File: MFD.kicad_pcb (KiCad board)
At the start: 2 copper layers, 209.6 x 209.6 mm, 43 parts, among them U1 4051, U2 ProMicro

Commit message: Adds OpenHardware Logo and GitHub link
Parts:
- added REF**: OSHW-Logo_7.5x8mm_SilkScreen, Symbol:OSHW-Logo_7.5x8mm_SilkScreen, F.Cu at (163.0, 52.2)
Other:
- board text added: "JLCJLCJLCJLC"
- board text added: "https://github.com/FalcoGer/AH64MFD-PCB"

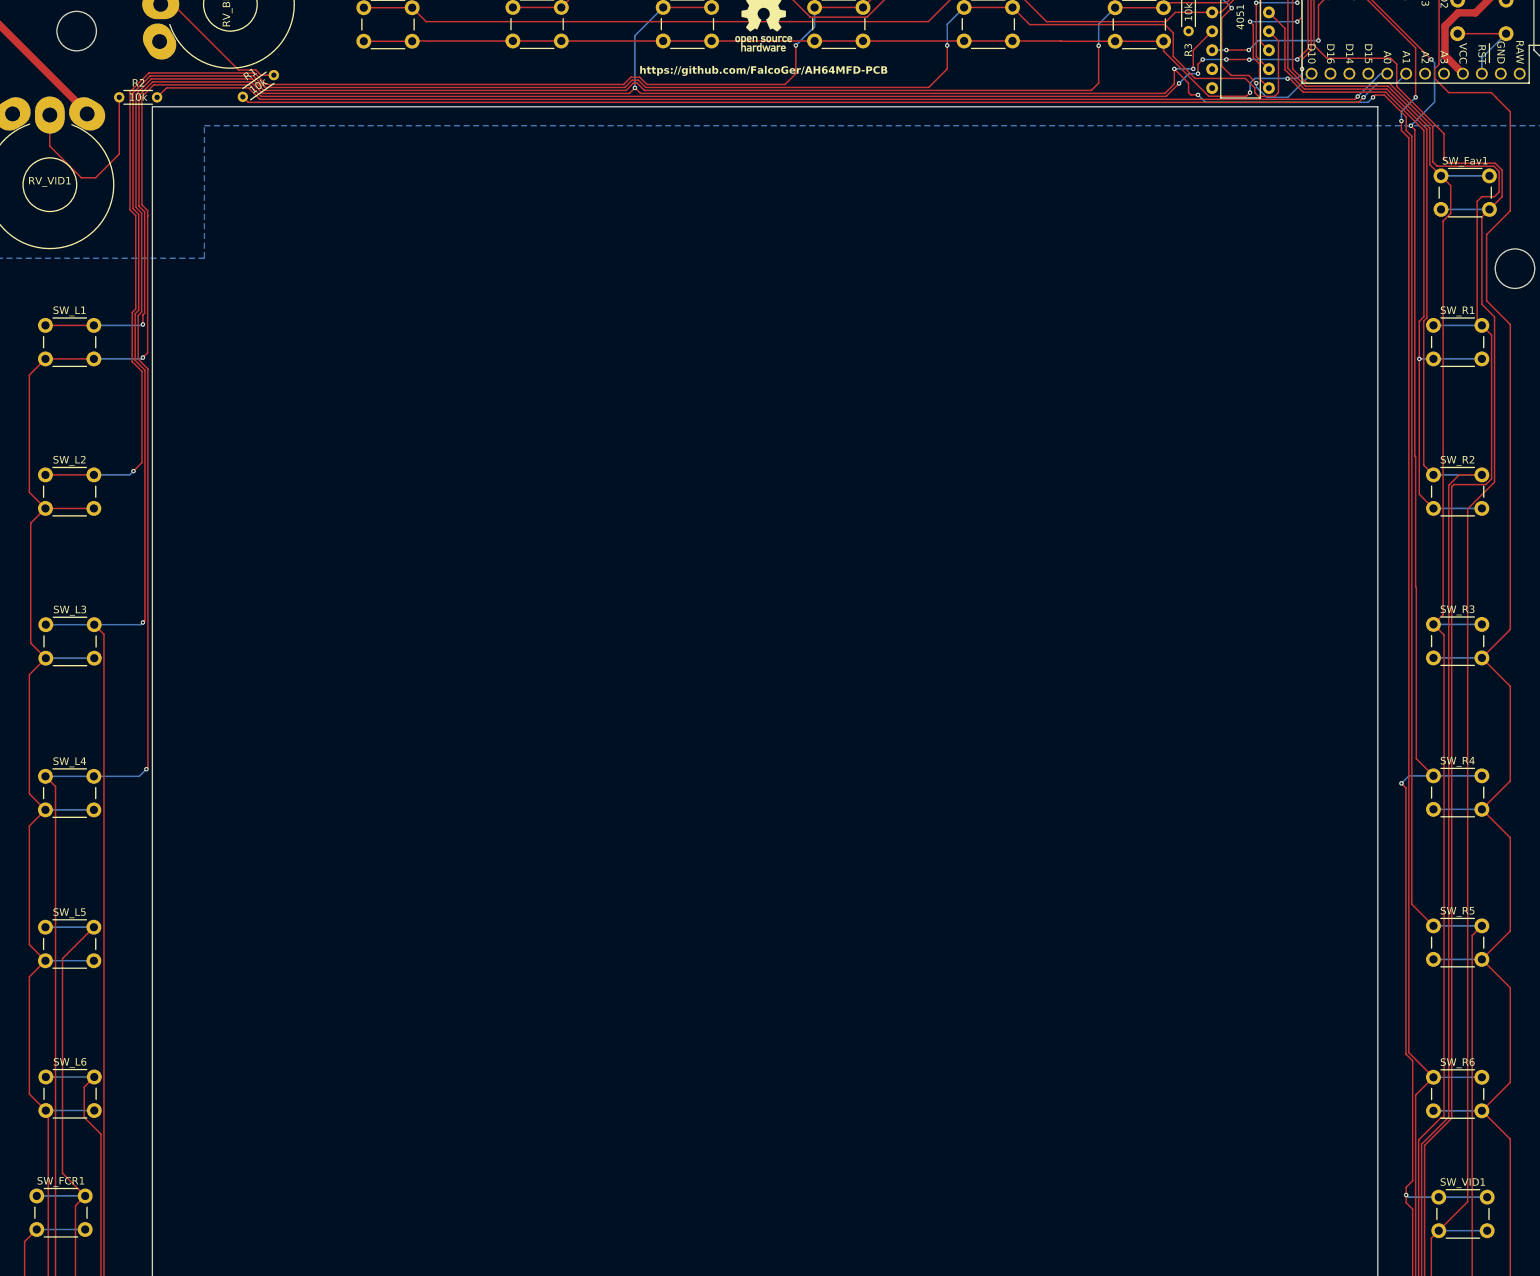
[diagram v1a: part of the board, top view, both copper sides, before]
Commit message: rerouted some tracks to use less vias.
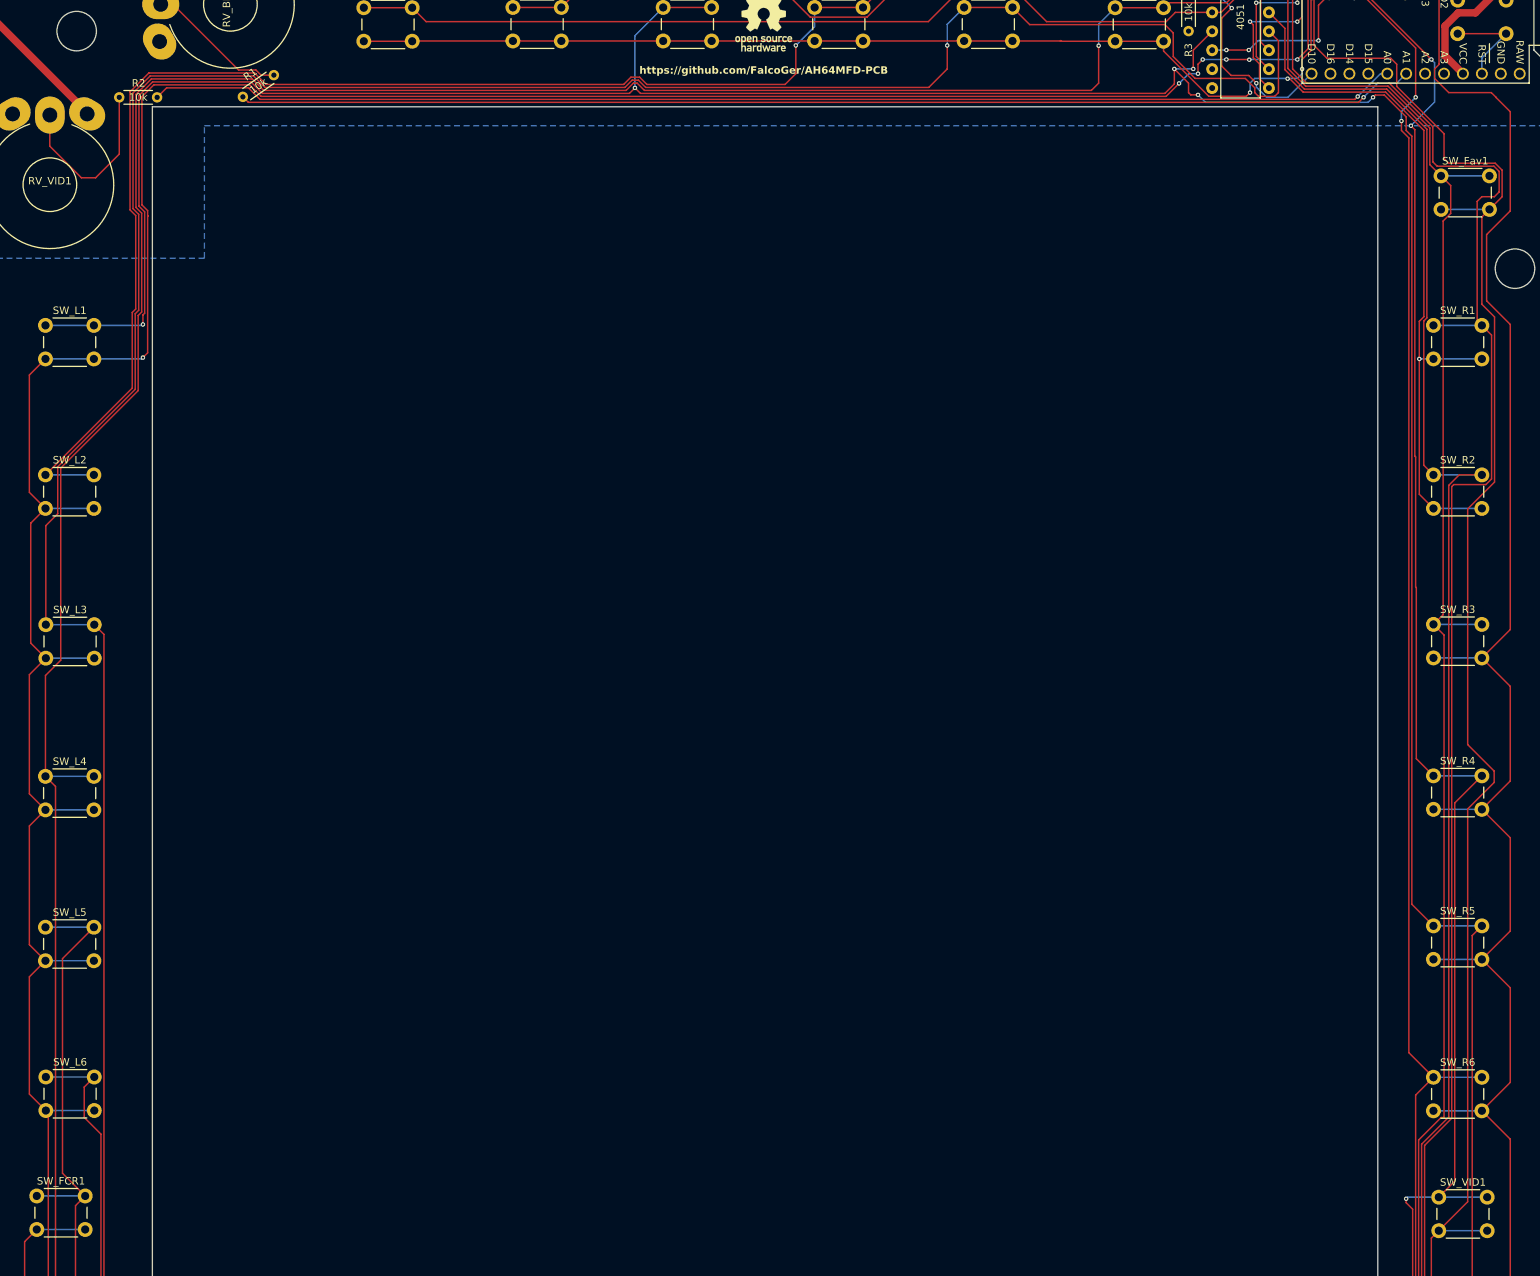
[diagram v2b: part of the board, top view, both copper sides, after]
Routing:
- net Net-(U2-D5): track 483.5 -> 486.4 mm
- net Net-(U1-X6): track 378.4 -> 375.9 mm, vias 8 -> 7
- net Net-(U1-X3): track 406.9 -> 404.9 mm, vias 2 -> 1
- net Net-(U1-X2): track 423.0 -> 421.0 mm, vias 2 -> 1
- net Net-(U1-X4): track 464.4 -> 463.2 mm, vias 8 -> 7

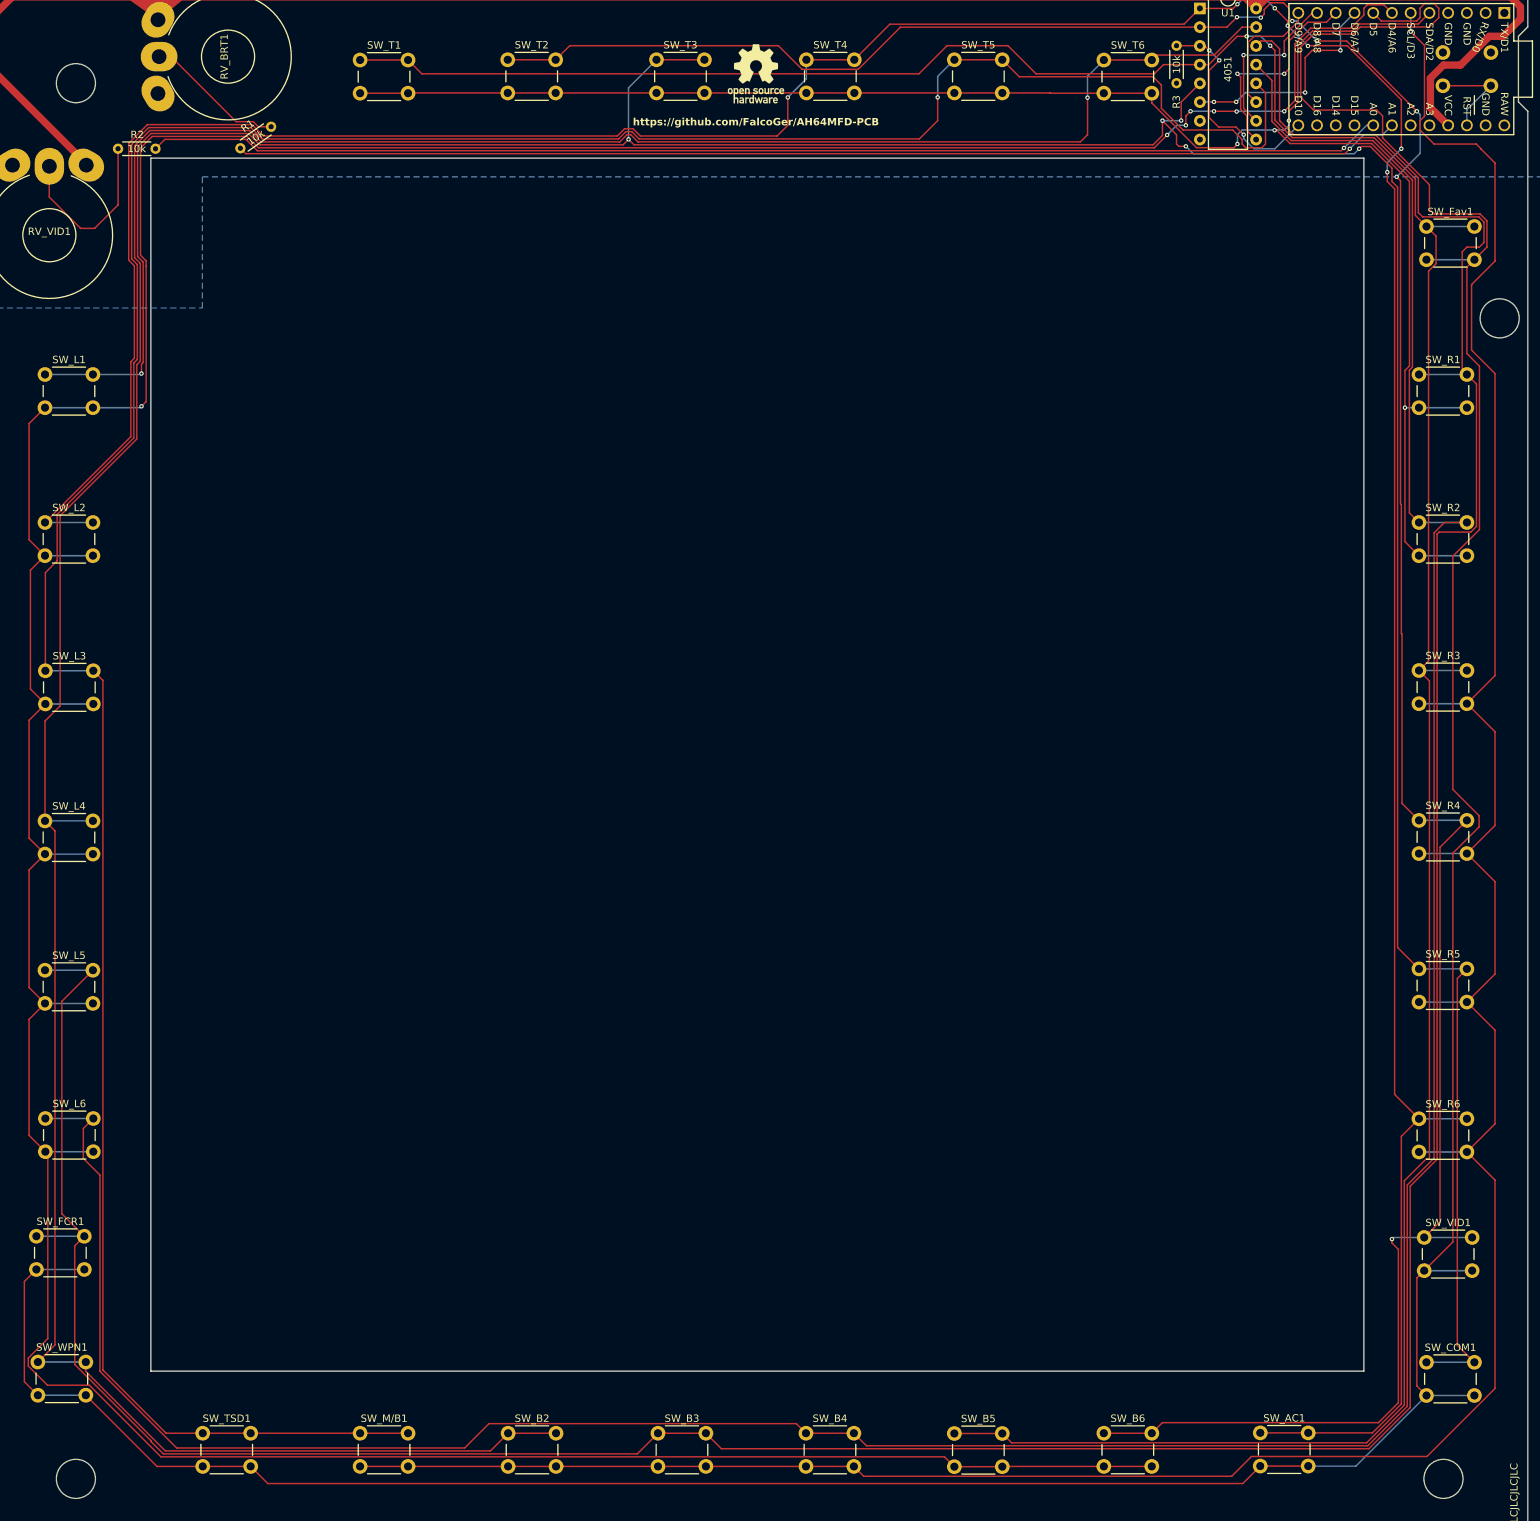
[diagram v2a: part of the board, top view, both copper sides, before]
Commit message: Adds mounting holes to schematic\nReroutes some tracks
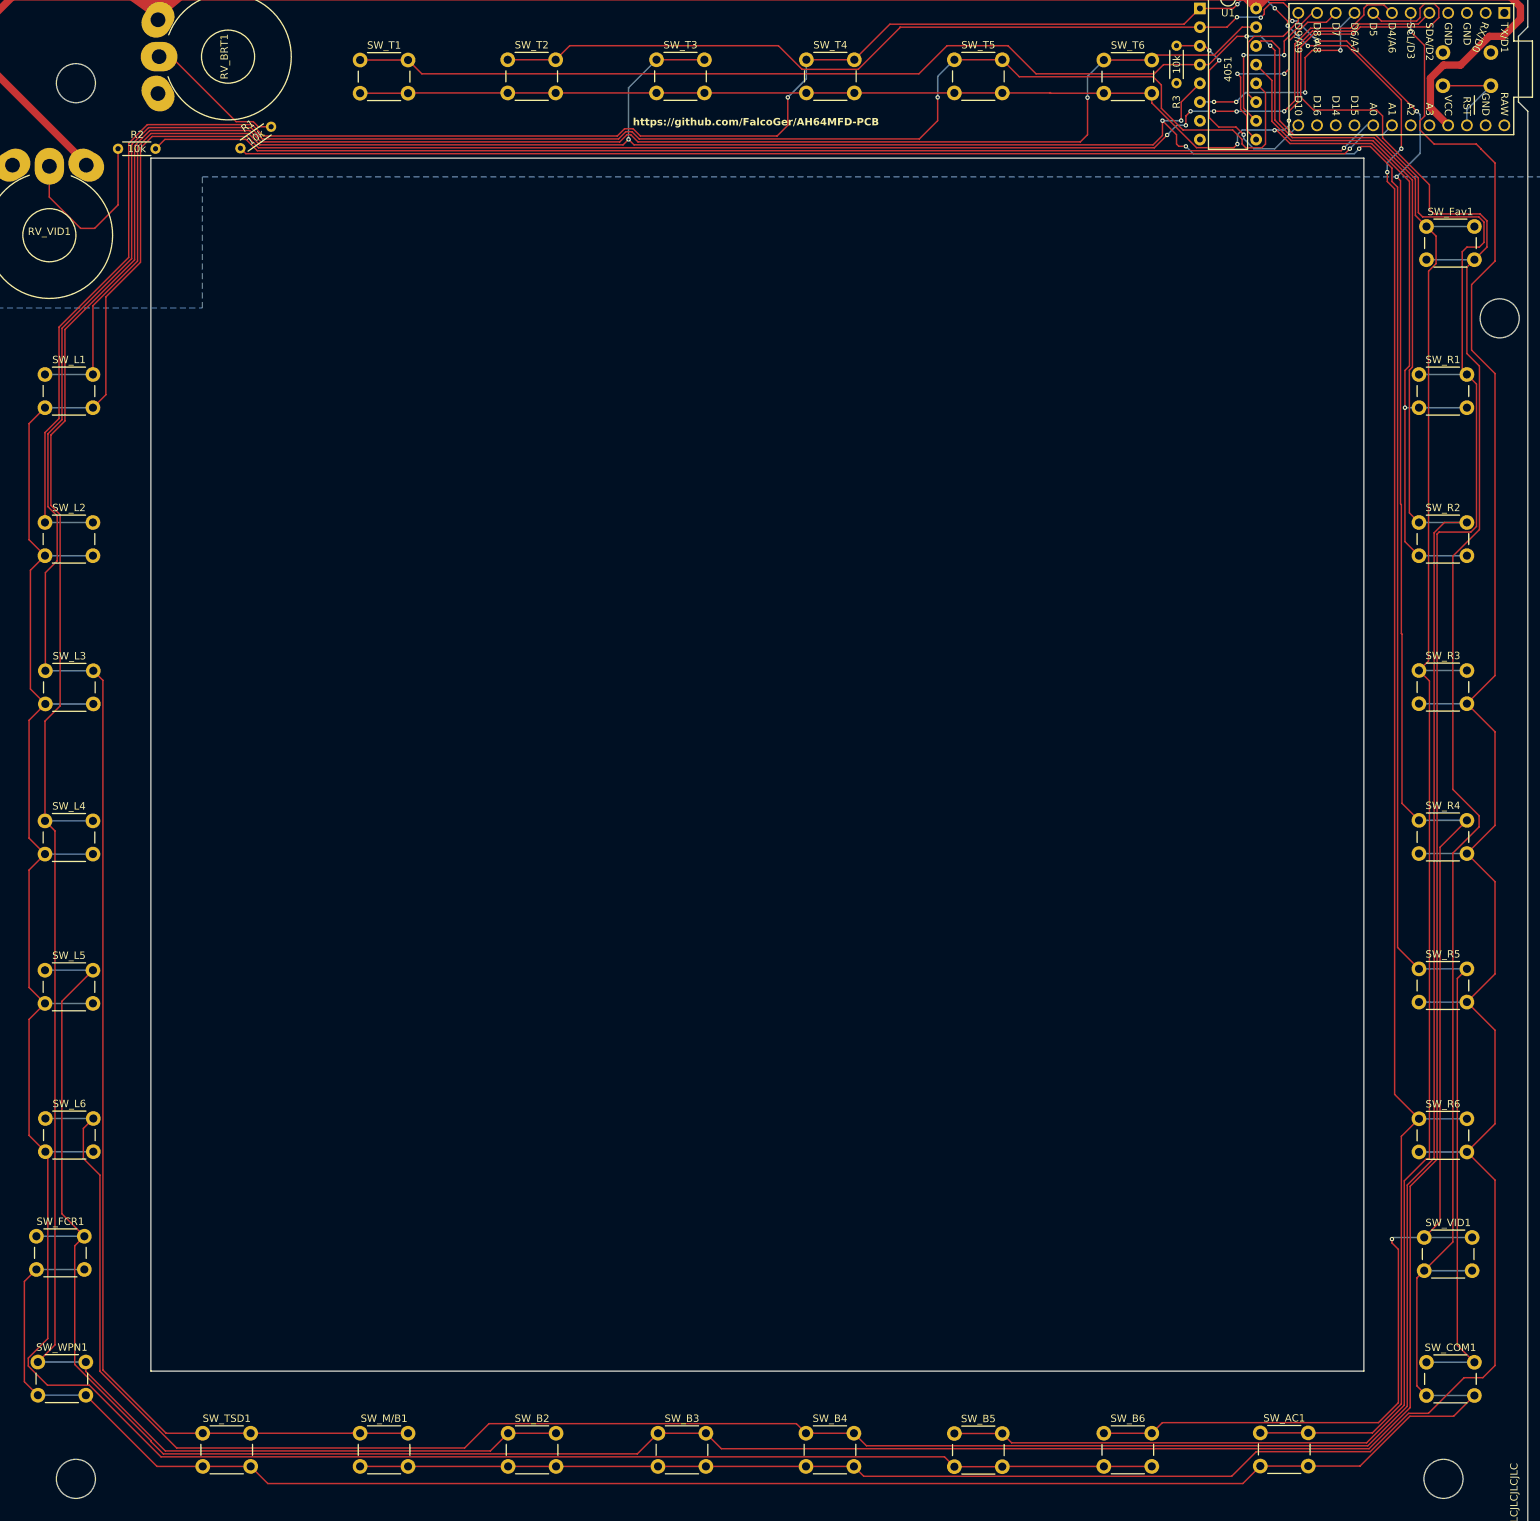
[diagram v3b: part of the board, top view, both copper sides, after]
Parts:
- removed REF**: OSHW-Logo_7.5x8mm_SilkScreen, Symbol:OSHW-Logo_7.5x8mm_SilkScreen
- H1, H2, H3, H4: renamed from REF**; value MountingHole_5.3mm_M5 -> MountingHole
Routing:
- net Net-(U2-D5): track 486.4 -> 492.9 mm
- net Net-(U1-X5): track 428.5 -> 424.1 mm, vias 6 -> 5
- net Net-(U2-D4/A6): track 564.0 -> 559.6 mm, vias 7 -> 6
- net Net-(U2-SCL/D3): track 395.7 -> 393.9 mm
- net Net-(U1-X4): track 463.2 -> 462.6 mm

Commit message: Ground plane over everything Rerouted some tracks, less vias
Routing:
- net Net-(U1-X3): track 405.3 -> 408.6 mm, vias 1 -> 0
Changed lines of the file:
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@@
 	)
 	(segment
-		(start 196.427999 54.800002)
-		(end 189.927999 54.800002)
-		(width 0.2)
-		(layer "F.Cu")
-		(net 6)
-	)
-	(segment
 		(start 216.695999 56.151637)
 		(end 222.764364 62.220002)
@@
 	)
 	(segment
+		(start 196.427999 54.800002)
+		(end 189.927999 54.800002)
+		(width 0.2)
+		(layer "B.Cu")
+		(net 6)
+	)
+	(segment
 		(start 259.419999 117.538002)
 		(end 252.919999 117.538002)
@@
 	)
 	(segment
+		(start 191.728999 52.101002)
+		(end 191.728999 57.031002)
+		(width 0.2)
+		(layer "F.Cu")
+		(net 29)
+	)
+	(segment
+		(start 187.724999 61.035002)
+		(end 184.870999 61.035002)
+		(width 0.2)
+		(layer "F.Cu")
+		(net 29)
+	)
+	(segment
 		(start 68.938999 99.106688)
 		(end 67.033999 101.011688)
@@
 	)
 	(segment
-		(start 187.664999 58.555002)
-		(end 185.184999 61.035002)
-		(width 0.2)
-		(layer "F.Cu")
-		(net 29)
-	)
-	(segment
 		(start 68.284999 118.245002)
 		(end 66.685999 119.844002)
@@
 	)
 	(segment
+		(start 191.728999 57.031002)
+		(end 187.724999 61.035002)
+		(width 0.2)
+		(layer "F.Cu")
+		(net 29)
+	)
+	(segment
 		(start 144.400784 61.035002)
 		(end 96.087057 61.035002)
@@
 	)
 	(segment
+		(start 189.927999 50.300002)
+		(end 191.728999 52.101002)
+		(width 0.2)
+		(layer "F.Cu")
+		(net 29)
+	)
+	(segment
 		(start 88.021999 236.518002)
 		(end 94.521999 236.518002)
@@
 	)
 	(segment
-		(start 189.927999 50.300002)
-		(end 196.427999 50.300002)
-		(width 0.2)
-		(layer "F.Cu")
-		(net 29)
-	)
-	(segment
-		(start 187.664999 55.400002)
-		(end 187.664999 58.555002)
-		(width 0.2)
-		(layer "F.Cu")
-		(net 29)
-	)
-	(segment
 		(start 83.052999 236.518002)
 		(end 88.021999 236.518002)
@@
 		(net 29)
 	)
-	(via
-		(at 187.664999 55.400002)
-		(size 0.6)
-		(drill 0.3)
-		(layers "F.Cu" "B.Cu")
-		(net 29)
-	)
 	(segment
 		(start 66.685999 133.140002)
@@
 	)
 	(segment
-		(start 187.664999 52.563002)
-		(end 187.664999 55.400002)
-		(width 0.2)
-		(layer "B.Cu")
-		(net 29)
-	)
-	(segment
 		(start 189.927999 50.300002)
-		(end 187.664999 52.563002)
+		(end 196.427999 50.300002)
 		(width 0.2)
 		(layer "B.Cu")
@@
 		(polygon
 			(pts
-				(xy 279.733886 34.878029) (xy 53.673886 34.878029) (xy 53.679999 83.955002) (xy 87.969999 83.955002)
-				(xy 87.969999 66.175002) (xy 279.739999 66.175002)
+				(xy 278.596999 32.647002) (xy 42.122999 32.901002) (xy 42.376999 268.359002) (xy 278.596999 268.359002)
 			)
 		)
